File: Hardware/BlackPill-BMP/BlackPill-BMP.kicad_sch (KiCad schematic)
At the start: 40 parts, among them J1 JTAG, J2 VCC, J3 GND, J4 SWO, J5 GDB_COMM, J6 TVCC, J7 LogicAna, J8 Conn_01x10, J9 Conn_01x11, U1 BlueAndBlackPill, U2 AD8531ARTZ, U3 SRV05-4, U4 TXS0108EPW, U5 SRV05-4

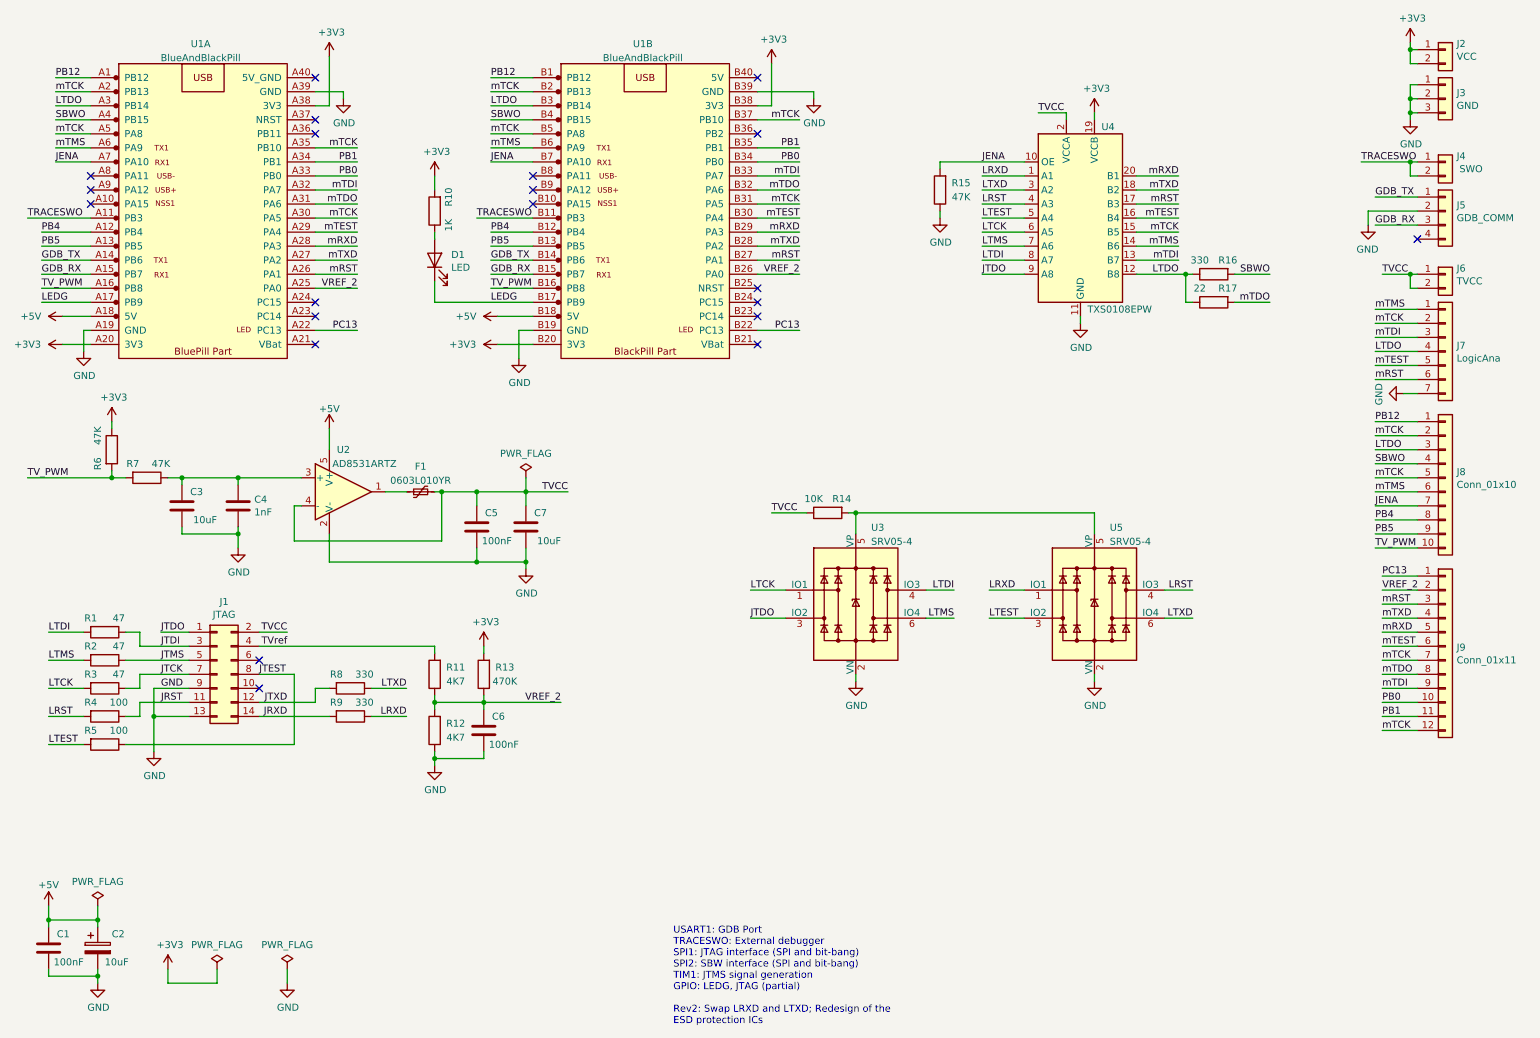
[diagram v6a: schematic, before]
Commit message: Swap mTMS and JENA pins for optimized DMA use in BluePill variant.
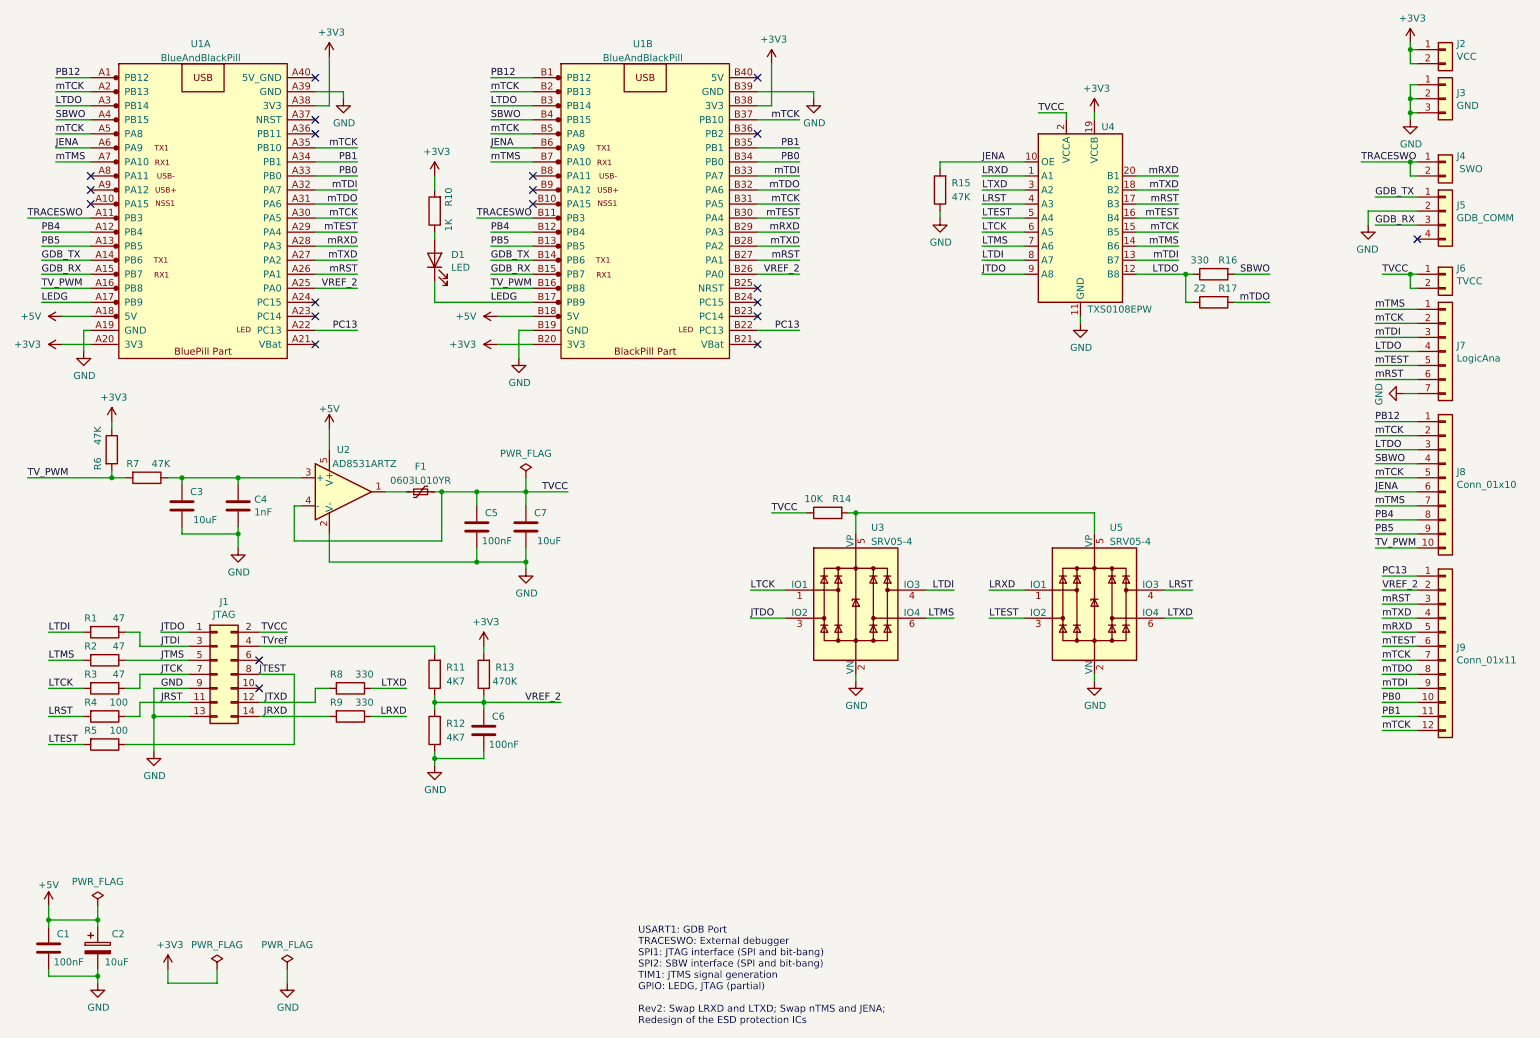
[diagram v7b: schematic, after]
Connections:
- net JENA: now also J8.6 (Pin_6), U1.A6 (PA9), U1.B6 (PA9); no longer J8.7 (Pin_7), U1.A7 (PA10), U1.B7 (PA10)
- net mTMS: now also J8.7 (Pin_7), U1.A7 (PA10), U1.B7 (PA10); no longer J8.6 (Pin_6), U1.A6 (PA9), U1.B6 (PA9)
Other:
- note added: "USART1: GDB Port TRACESWO: External debugger SPI1: JTAG interface (SPI and bit-bang) SPI2: SBW interface (SPI and bit-bang) TIM1: JTMS signal generation GPIO: LEDG, JTAG (partial) Rev2: Swap LRXD and LTXD; Swap nTMS and JENA; Redesign of the ESD protection ICs"
- note removed: "USART1: GDB Port TRACESWO: External debugger SPI1: JTAG interface (SPI and bit-bang) SPI2: SBW interface (SPI and bit-bang) TIM1: JTMS signal generation GPIO: LEDG, JTAG (partial) Rev2: Swap LRXD and LTXD; Redesign of the ESD protection ICs"
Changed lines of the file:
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@@
   (title_block
     (title "MSPBMP Development Protoboard")
-    (date "2022-08-21")
+    (date "2022-08-23")
     (rev "2")
     (company "Mathias Gruber")
@@
     (stroke (width 0) (type default) (color 0 0 0 0))
   )
-  (text "USART1: GDB Port\nTRACESWO: External debugger\nSPI1: JTAG interface (SPI and bit-bang)\nSPI2: SBW interface (SPI and bit-bang)\nTIM1: JTMS signal generation\nGPIO: LEDG, JTAG (partial)\n\nRev2: Swap LRXD and LTXD; Redesign of the \nESD protection ICs"
-    (at 132.08 196.85 0)
+  (text "USART1: GDB Port\nTRACESWO: External debugger\nSPI1: JTAG interface (SPI and bit-bang)\nSPI2: SBW interface (SPI and bit-bang)\nTIM1: JTMS signal generation\nGPIO: LEDG, JTAG (partial)\n\nRev2: Swap LRXD and LTXD; Swap nTMS and JENA;\nRedesign of the ESD protection ICs"
+    (at 125.73 196.85 0)
     (effects (font (size 1.27 1.27)) (justify left bottom))
   )
@@
     (effects (font (size 1.27 1.27)) (justify left bottom))
   )
-  (label "mTMS" (at 20.32 38.1 0)
+  (label "mTMS" (at 20.32 40.64 0)
     (effects (font (size 1.27 1.27)) (justify left bottom))
   )
@@
     (effects (font (size 1.27 1.27)) (justify right bottom))
   )
-  (label "JENA" (at 259.08 102.87 0)
+  (label "JENA" (at 259.08 100.33 0)
     (effects (font (size 1.27 1.27)) (justify left bottom))
   )
@@
     (effects (font (size 1.27 1.27)) (justify right bottom))
   )
-  (label "mTMS" (at 99.06 38.1 0)
+  (label "mTMS" (at 99.06 40.64 0)
     (effects (font (size 1.27 1.27)) (justify left bottom))
   )
@@
     (effects (font (size 1.27 1.27)) (justify left bottom))
   )
-  (label "JENA" (at 99.06 40.64 0)
-    (effects (font (size 1.27 1.27)) (justify left bottom))
-  )
-  (label "mTMS" (at 259.08 100.33 0)
+  (label "JENA" (at 99.06 38.1 0)
+    (effects (font (size 1.27 1.27)) (justify left bottom))
+  )
+  (label "mTMS" (at 259.08 102.87 0)
     (effects (font (size 1.27 1.27)) (justify left bottom))
   )
@@
     (effects (font (size 1.27 1.27)) (justify left bottom))
   )
-  (label "JENA" (at 20.32 40.64 0)
-    (effects (font (size 1.27 1.27)) (justify left bottom))
-  )
+  (label "JENA" (at 20.32 38.1 0)
+    (effects (font (size 1.27 1.27)) (justify left bottom))
+  )

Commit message: Changed TXS0108 for TXB0304. for lower impedance. Using ESD protection of those parts.
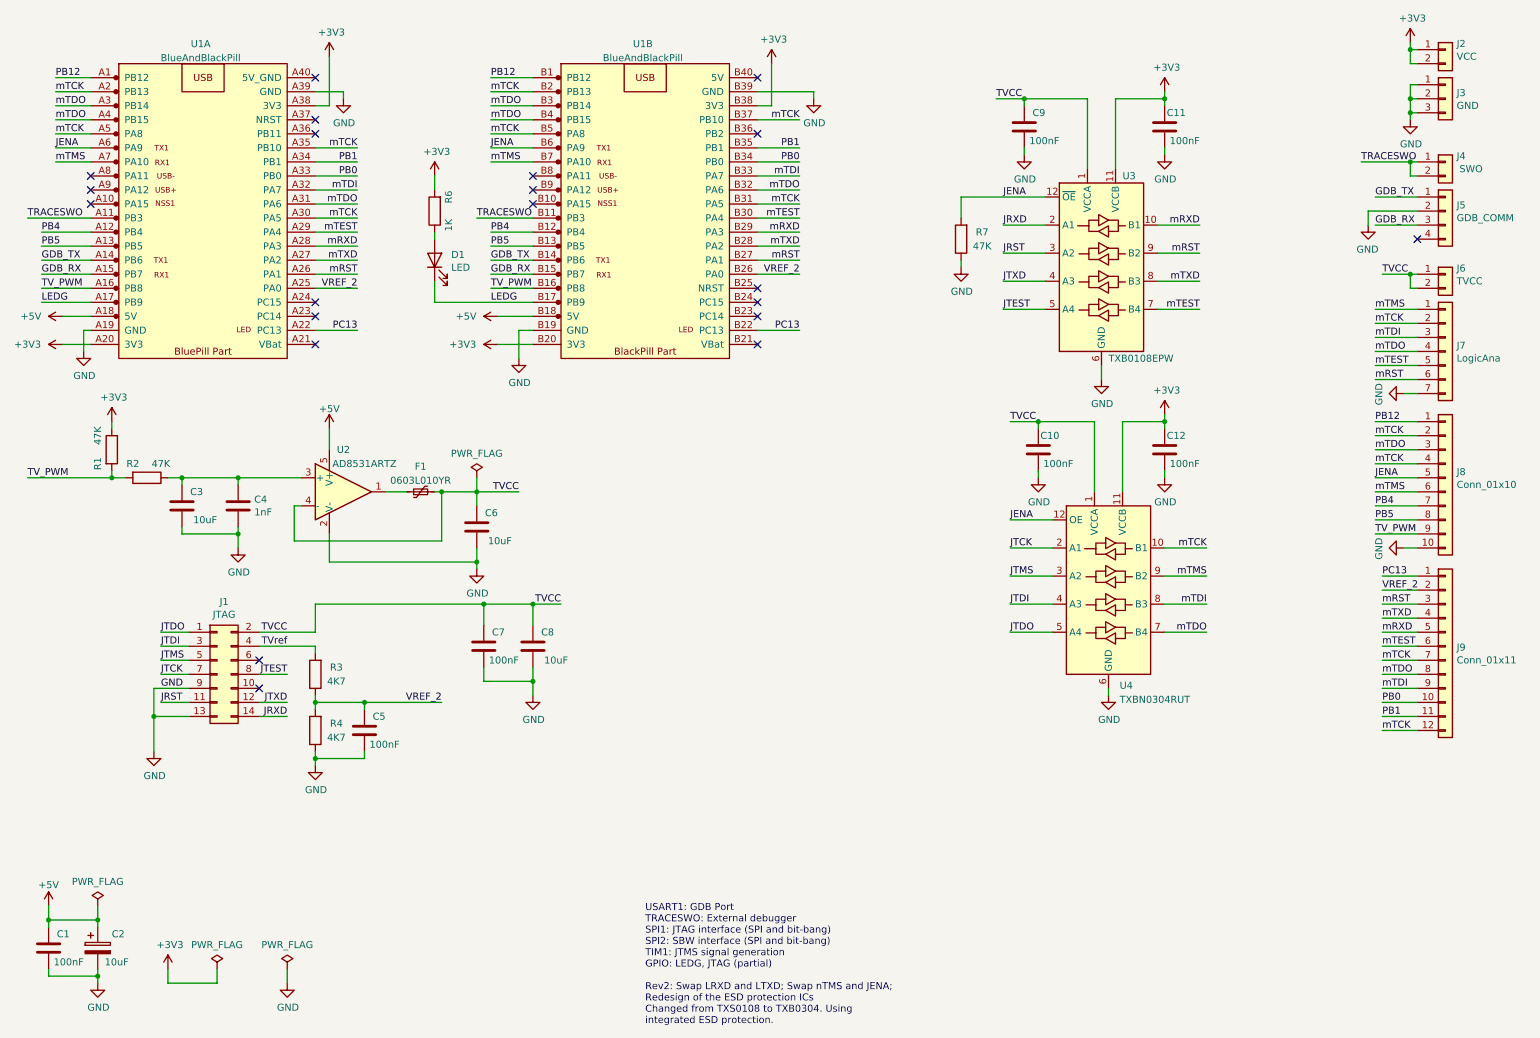
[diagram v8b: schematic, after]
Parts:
- removed R1, R2, R3: 47, Resistor_SMD:R_0603_1608Metric_Pad0.98x0.95mm_HandSolder, symbol Device:R
- removed R13: 470K, Resistor_SMD:R_0603_1608Metric_Pad0.98x0.95mm_HandSolder, symbol Device:R
- removed R14: 10K, Resistor_SMD:R_0603_1608Metric_Pad0.98x0.95mm_HandSolder, symbol Device:R
- removed R16, R8, R9: 330, Resistor_SMD:R_0603_1608Metric_Pad0.98x0.95mm_HandSolder, symbol Device:R
- removed R17: 22, Resistor_SMD:R_0603_1608Metric_Pad0.98x0.95mm_HandSolder, symbol Device:R
- removed R4, R5: 100, Resistor_SMD:R_0603_1608Metric_Pad0.98x0.95mm_HandSolder, symbol Device:R
- removed U3, U5: SRV05-4, Package_TO_SOT_SMD:SOT-23-6_Handsoldering, symbol Power_Protection:SRV05-4
- added C10, C11, C12, C9: 100nF, Capacitor_SMD:C_0603_1608Metric_Pad1.08x0.95mm_HandSolder, symbol Device:C
- added C8: 10uF, Capacitor_SMD:C_0603_1608Metric_Pad1.08x0.95mm_HandSolder, symbol Device:C
- added U4: TXBN0304RUT, Package_DFN_QFN:Texas_R_PUQFN-N12, symbol Logic_LevelTranslator:TXB0304RUT
- U3: renamed from U4; value TXS0108EPW -> TXB0108EPW; footprint Package_SO:TSSOP-20_4.4x6.5mm_P0.65mm -> Package_DFN_QFN:Texas_R_PUQFN-N12; symbol Logic_LevelTranslator:TXS0108EPW -> Logic_LevelTranslator:TXBN0304RUT
- renumbered C6 to C5, C7 to C6, C5 to C7, R6 to R1, R7 to R2, R11 to R3, R12 to R4, R10 to R6, R15 to R7
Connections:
- net LRST is gone; now on net JTXD: U3.4 (A3)
- net LRXD is gone; now on net TVCC: U3.1 (VCCA)
- net LTCK is gone; now on net GND: U3.6 (GND)
- net LTDI is gone; now on net mTXD: U3.8 (B3)
- net LTEST is gone; now on net JTEST: U3.5 (A4)
- net LTMS is gone; now on net mTEST: U3.7 (B4)
- net LTXD is gone; now on net JRST: U3.3 (A2)
- net +3V3: now also U3.11 (VCCB), C11.2, C12.2, U4.11 (VCCB); no longer U3.19 (VCCB)
- net GND: now also J8.10 (Pin_10), C10.1, C11.1, C12.1, C8.1, C9.1, U4.6 (GND); no longer U3.11 (GND)
- net JENA: now also J8.5 (Pin_5), U3.12 (~{OE}), U4.12 (OE); no longer J8.6 (Pin_6), U3.10 (OE)
- net JRXD: now also U3.2 (A1)
- net JTCK: now also U4.2 (A1)
- net JTDI: now also U4.4 (A3)
- net JTDO: now also U4.5 (A4); no longer U3.9 (A8)
- net JTMS: now also U4.3 (A2)
- net PB4: now also J8.7 (Pin_7); no longer J8.8 (Pin_8)
- net PB5: now also J8.8 (Pin_8); no longer J8.9 (Pin_9)
- net TVCC: now also C10.2, C8.2, C9.2, U4.1 (VCCA); no longer U3.2 (VCCA)
- net TV_PWM: now also J8.9 (Pin_9); no longer J8.10 (Pin_10)
- net mRST: now also U3.9 (B2); no longer U3.17 (B3)
- net mRXD: now also U3.10 (B1); no longer U3.20 (B1)
- net mTCK: now also J8.4 (Pin_4), U4.10 (B1); no longer J8.5 (Pin_5), U3.15 (B5)
- net mTDI: now also U4.8 (B3); no longer U3.13 (B7)
- net mTDO: now also J7.4 (Pin_4), J8.3 (Pin_3), U1.A3 (PB14), U1.A4 (PB15), U1.B3 (PB14), U1.B4 (PB15), U4.7 (B4)
- net mTEST: no longer U3.16 (B4)
- net mTMS: now also J8.6 (Pin_6), U4.9 (B2); no longer J8.7 (Pin_7), U3.14 (B6)
- net mTXD: no longer U3.18 (B2)
- removed net LTDO: J7.4 (Pin_4), J8.3 (Pin_3), U1.A3 (PB14), U1.B3 (PB14), U3.12 (B8)
- removed net SBWO: J8.4 (Pin_4), U1.A4 (PB15), U1.B4 (PB15)
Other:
- note added: "USART1: GDB Port TRACESWO: External debugger SPI1: JTAG interface (SPI and bit-bang) SPI2: SBW interface (SPI and bit-bang) TIM1: JTMS signal generation GPIO: LEDG, JTAG (partial) Rev2: Swap LRXD and LTXD; Swap nTMS and JENA; Redesign of the ESD protection ICs Changed from TXS0108 to TXB0304. Using integrated ESD protection."
- note removed: "USART1: GDB Port TRACESWO: External debugger SPI1: JTAG interface (SPI and bit-bang) SPI2: SBW interface (SPI and bit-bang) TIM1: JTMS signal generation GPIO: LEDG, JTAG (partial) Rev2: Swap LRXD and LTXD; Swap nTMS and JENA; Redesign of the ESD protection ICs"
- moved on the sheet: C5, C6, C7, R3, R4, R7, U3
